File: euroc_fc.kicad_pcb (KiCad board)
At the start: 4 copper layers, 50 x 100 mm, 143 parts, among them J1 Micro-Fit, J10 USB_C_Receptacle_USB2.0, J11 Pin Header, J2 Micro-Fit, J3 Micro-Fit, J4 SMA, J5 JST-GH, J6 JST-GH, J7 JST-GH, J8 JST-GH, J9 Micro_SD_Card_Det, Q1 DMN2056U, Q2 AOSP21321, Q3 DMN2056U, Q4 AOSP21321, Q5 DMN2056U, Q6 DMN2056U, Q7 DMN2056U, SW1 EVQ-PUC02K, SW2 EVQ-PUC02K, U1 STM32F401RCT6, U10 Ai-Thinker-Ra-01, U11 W25Q256JVF, U2 L7805, U3 L7805, U4 AZ1117I-3.3, U5 LSM6DSR, U6 ADXL375, U7 MS5611-01BA, U8 BMM150, U9 SAM-M8Q, Y1 25M

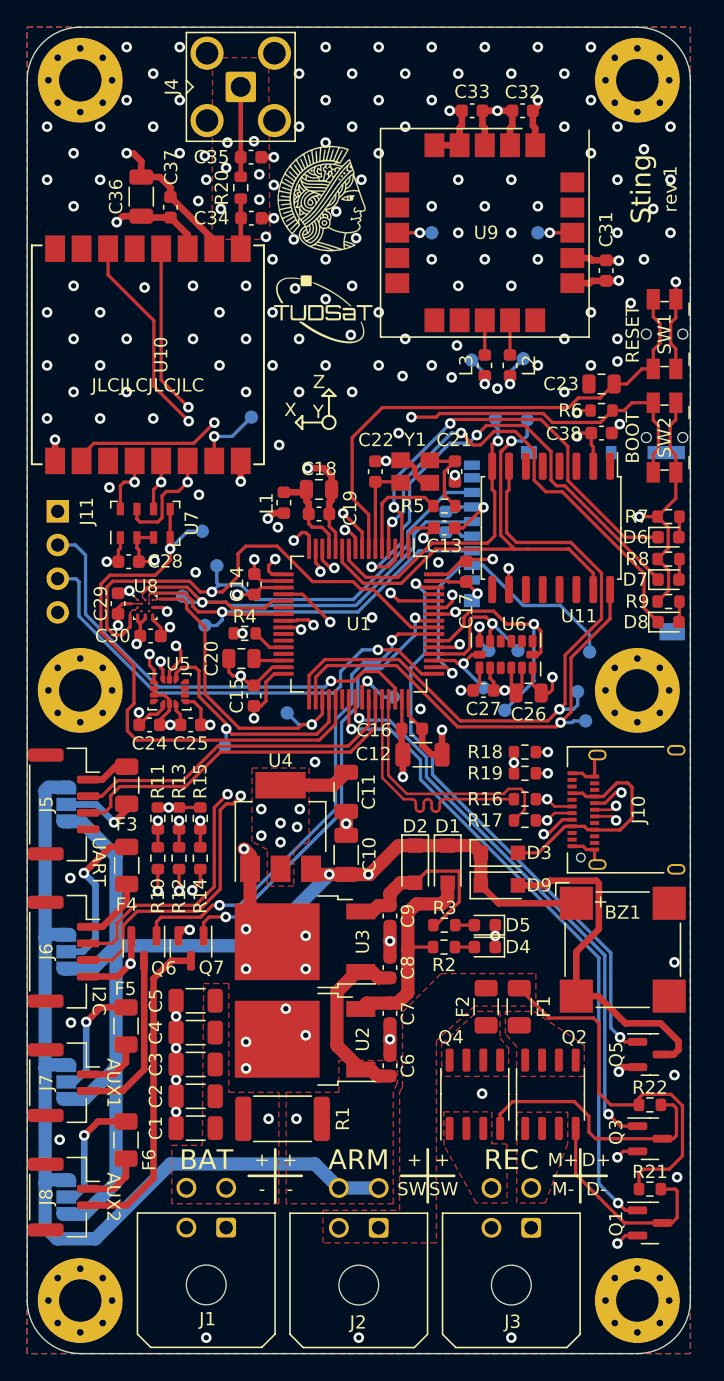
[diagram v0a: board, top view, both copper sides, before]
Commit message: Adjust cap value notation
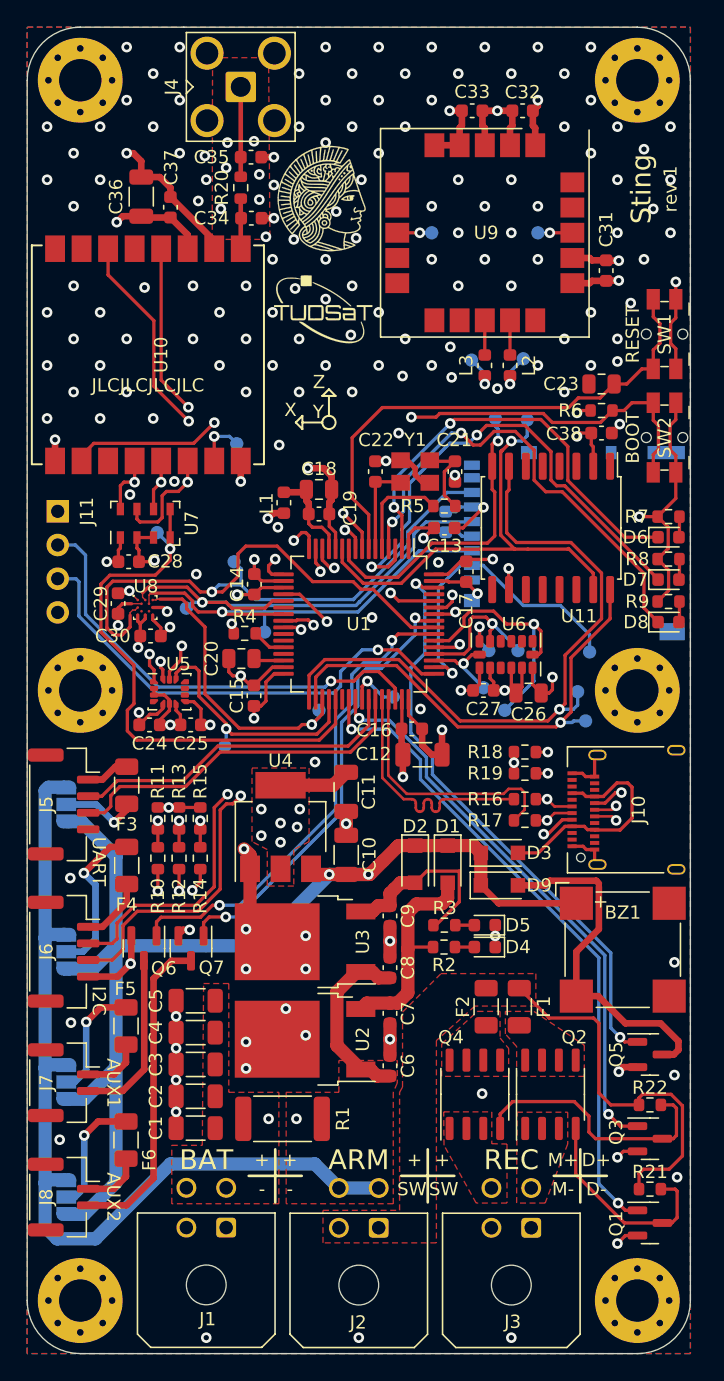
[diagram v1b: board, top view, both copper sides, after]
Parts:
- C12: value 4.7u -> 4u7
- C20, C23: value 2.2u -> 2u2
- J11: value Pin Header -> SWD Header
- R18, R19: value 5.1k -> 5k1
- moved TP2 4.53 mm to (92.9, 95.6)
- moved TP6 3.40 mm to (84.8, 88.1)
- moved TP5 2.41 mm to (97.0, 101.5)
- moved TP7 2.28 mm to (90.8, 81.4)
- moved TP3 1.33 mm to (90.6, 90.3)
- moved TP1 0.95 mm to (87.0, 93.8)
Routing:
- net SPI1_CS_RADIO: track 25.8 -> 24.3 mm
- net SPI1_CS_BARO: track 43.5 -> 42.1 mm
- net SPI1_CS_MAG: track 23.8 -> 22.9 mm
- net SPI1_SCL: track 62.1 -> 61.3 mm
- net SPI1_MOSI: track 62.3 -> 61.8 mm

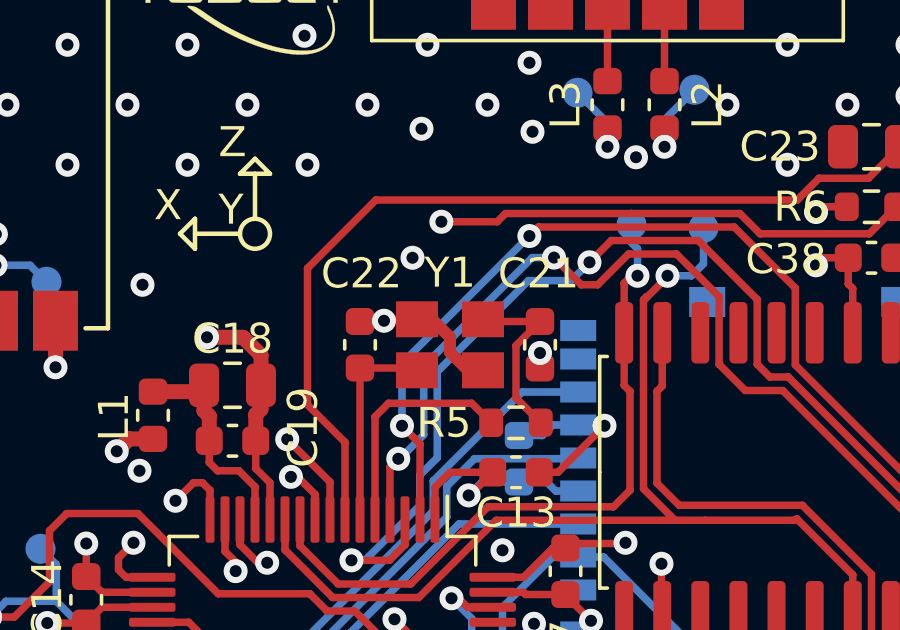
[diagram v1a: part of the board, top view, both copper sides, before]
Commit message: Replace crystal oscillator part
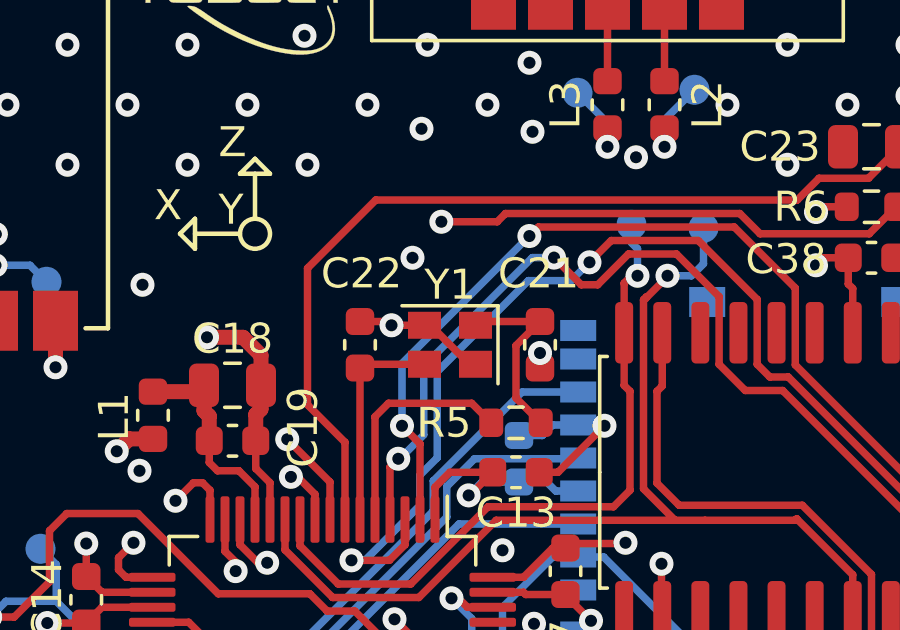
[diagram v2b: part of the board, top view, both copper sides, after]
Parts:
- Y1: footprint Crystal:Crystal_SMD_Abracon_ABM8G-4Pin_3.2x2.5mm -> Oscillator:Oscillator_SMD_SeikoEpson_SG210-4Pin_2.5x2.0mm
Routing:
- net GND: track 153.7 -> 152.9 mm

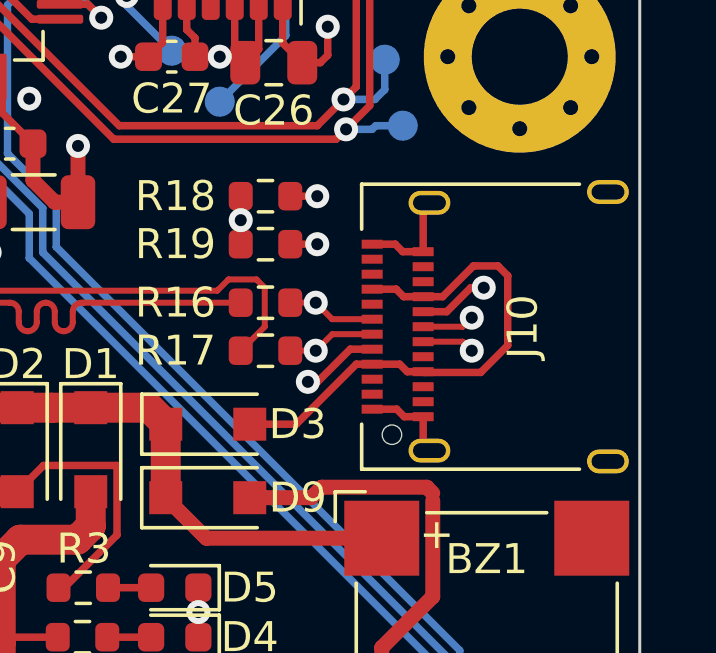
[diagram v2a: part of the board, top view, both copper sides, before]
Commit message: Replace USB connector
New part is cheaper, smaller, easier to solder and avilable at LCSC.
Also, don't ground the USB shield anymore.
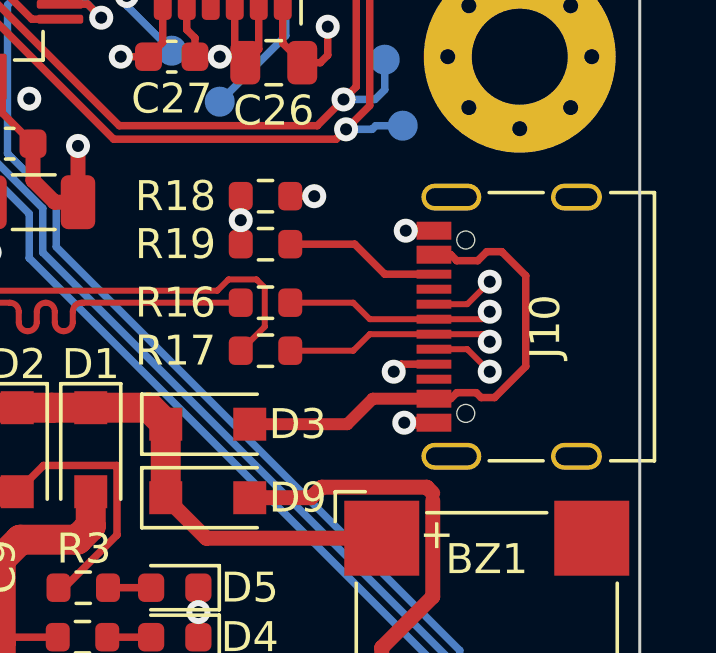
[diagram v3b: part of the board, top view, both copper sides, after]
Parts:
- J10: footprint Connector_USB:USB_C_Receptacle_Amphenol_12401610E4-2A -> Connector_USB:USB_C_Receptacle_Palconn_UTC16-G
- Y1: value 25M -> 25M, 18p
- moved J10 0.45 mm to (120.7, 109.0)
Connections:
- J10 pad S1: GND -> unconnected-(J10-PadS1)
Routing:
- net GND: track 152.9 -> 148.3 mm, vias 191 -> 193
- net Net-(J10-PadB5): track 9.40 -> 5.20 mm, vias 2 -> 0
- net /D0+: track 12.7 -> 11.7 mm
- net Net-(J10-PadA5): track 10.2 -> 9.19 mm
- net /D0-: track 12.7 -> 11.7 mm
- net Net-(D3-Pad2): track 17.4 -> 16.8 mm
